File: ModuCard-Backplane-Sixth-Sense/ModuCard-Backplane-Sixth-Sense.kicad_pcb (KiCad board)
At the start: 4 copper layers, 153.9 x 128.7 mm, 138 parts, among them J1 09031967921, J16 09031967921, J17 09031967921, J18 09031967921, J19 09031967921, J2 09031967921, J20 09031967921, J21 09031967921, J6 Conn_01x02_Pin, SW1 SW_DIP_x02, SW2 SW_DIP_x02, SW3 SW_DIP_x02, SW4 SW_DIP_x02, U1 LM5007MM, U3 AMS1117, U4 FE2.1, U801 FSUSB42UMX, U802 FSUSB42UMX, X2 X322512MSB4SI

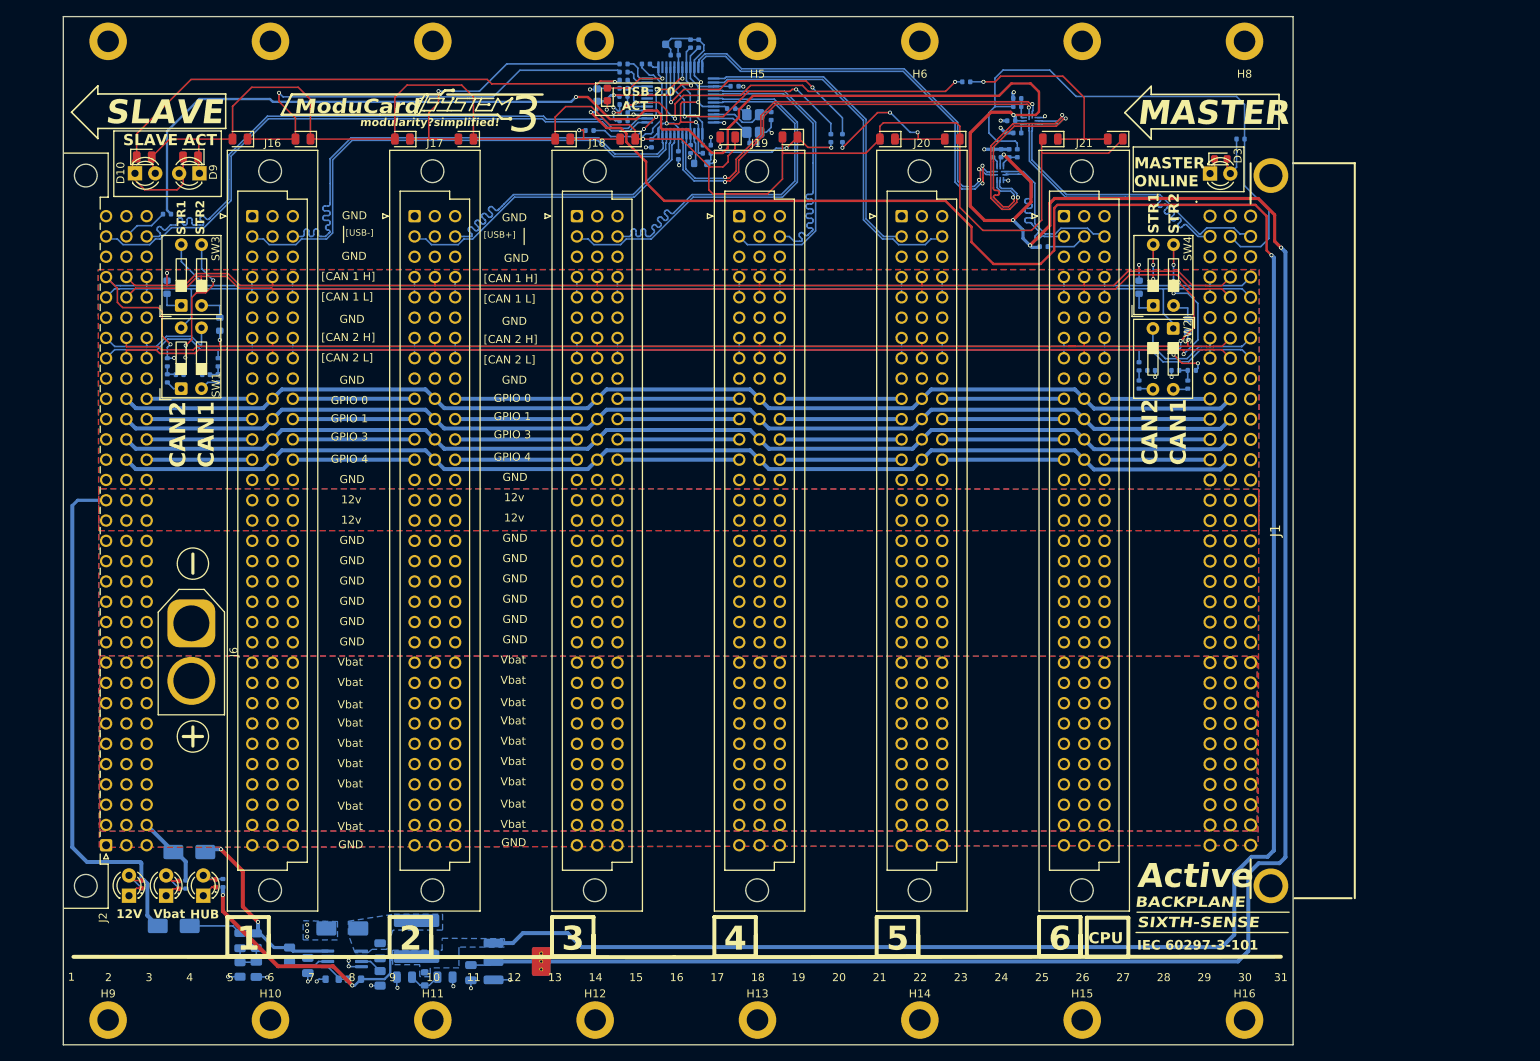
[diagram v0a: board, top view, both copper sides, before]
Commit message: fix DRC errors, change pinout
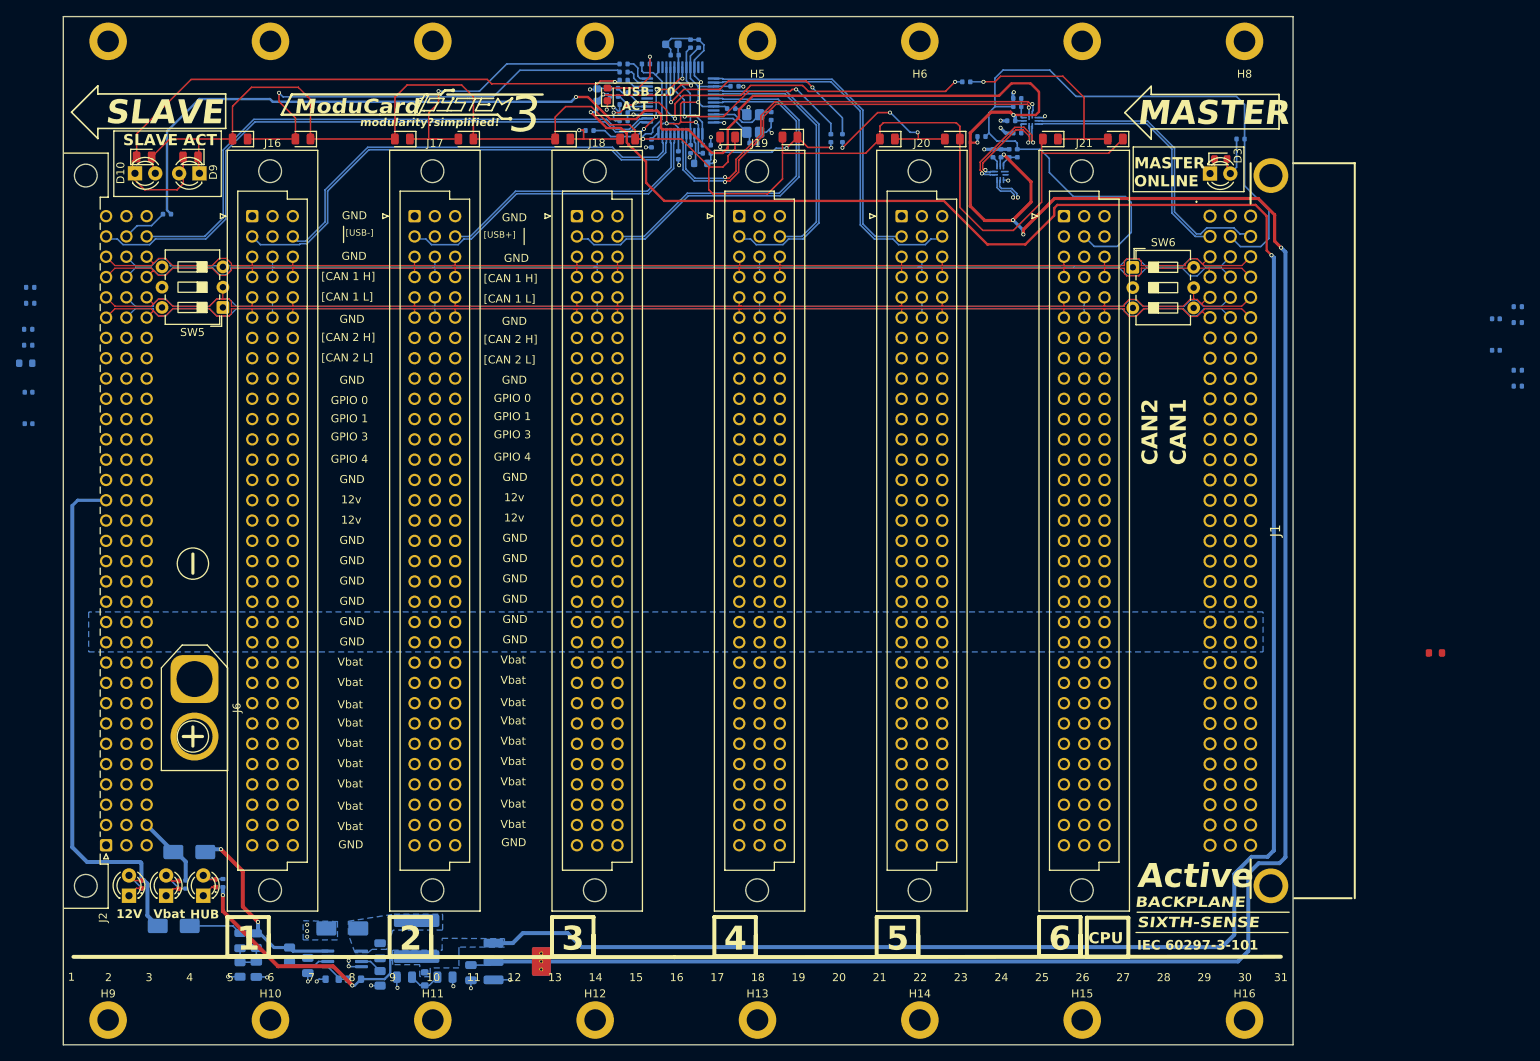
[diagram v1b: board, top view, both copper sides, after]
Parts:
- removed R21, R23: 100Ω, PCM_JLCPCB:R_0603
- removed R25: 1kΩ, PCM_JLCPCB:R_0402
- removed SW1, SW2, SW3, SW4: SW_DIP_x02, Button_Switch_THT:SW_DIP_SPSTx02_Slide_9.78x7.26mm_W7.62mm_P2.54mm
- added R2: 10kΩ, PCM_JLCPCB:R_0402, B.Cu at (204.8, 93.2)
- added R20: 10kΩ, PCM_JLCPCB:R_0402, B.Cu at (248.5, 98.8)
- added SW5: SW_DIP_x03, Button_Switch_THT:SW_DIP_SPSTx03_Slide_6.7x9.18mm_W7.62mm_P2.54mm_LowProfile, F.Cu at (153.6, 120.1)
- added SW6: SW_DIP_x03, Button_Switch_THT:SW_DIP_SPSTx03_Slide_6.7x9.18mm_W7.62mm_P2.54mm_LowProfile, F.Cu at (267.4, 115.1)
- R22: moved to F.Cu
- moved R5 169.2 mm to (315.6, 122.0), turned to 180 degrees
- moved R4 169.2 mm to (315.6, 120.0), turned to 180 degrees
- moved C21 164.9 mm to (312.9, 121.6), turned to 180 degrees
- moved R8 162.7 mm to (315.6, 128.0), turned to 180 degrees
- moved R9 162.7 mm to (315.6, 130.0), turned to 180 degrees
- moved C23 161.5 mm to (312.9, 125.5)
- moved R22 157.6 mm to (305.3, 163.4), turned to 0 degrees
- moved R7 145.6 mm to (129.4, 119.6), turned to 180 degrees
- moved R24 145.5 mm to (128.9, 127.1), turned to 180 degrees
- moved R6 145.4 mm to (129.4, 117.6), turned to 180 degrees
- moved C22 143.6 mm to (129.2, 130.8)
- moved C24 140.7 mm to (129.2, 134.7), turned to 180 degrees
- moved R10 139.2 mm to (129.2, 122.9), turned to 180 degrees
- moved R11 139.1 mm to (129.2, 124.9), turned to 180 degrees
- moved J6 6.98 mm to (150.0, 166.7)
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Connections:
- D10 pad 2: Net-(D10-A) -> /FE2.1/DRV
- D20 pad 2: Net-(D10-A) -> /FE2.1/DRV
- D21 pad 1: Net-(D10-A) -> /FE2.1/DRV
- D22 pad 2: Net-(D10-A) -> /FE2.1/DRV
- D23 pad 1: Net-(D10-A) -> /FE2.1/DRV
- D24 pad 2: Net-(D10-A) -> /FE2.1/DRV
- D25 pad 1: Net-(D10-A) -> /FE2.1/DRV
- D26 pad 2: Net-(D10-A) -> /FE2.1/DRV
- D27 pad 1: Net-(D10-A) -> /FE2.1/DRV
- D28 pad 2: Net-(D10-A) -> /FE2.1/DRV
- D29 pad 1: Net-(D10-A) -> /FE2.1/DRV
- D30 pad 2: Net-(D10-A) -> /FE2.1/DRV
- D31 pad 1: Net-(D10-A) -> /FE2.1/DRV
- D32 pad 1: Net-(D10-A) -> /FE2.1/DRV
- D33 pad 2: Net-(D10-A) -> /FE2.1/DRV
- D34 pad 2: /FE2.1/DRV -> Net-(D34-Pad2)
- D9 pad 1: Net-(D10-A) -> /FE2.1/DRV
- J1 pad A10: /Ext-conn-M/GPIOL0 -> /Ext-conn-M/GPIOL3
- J1 pad A11: /Ext-conn-M/GPIOL1 -> /Ext-conn-M/GPIOL4
- J1 pad A12: /Ext-conn-M/GPIOL2 -> /Ext-conn-M/GPIOL5
- J1 pad A13: /Ext-conn-M/GPIOL3 -> /Ext-conn-M/GPIOL6
- J1 pad A14: GND -> /Ext-conn-M/GPIOL7
- J1 pad A15: +12V -> /Ext-conn-M/GPIOL8
- J1 pad A16: +12V -> /Ext-conn-M/GPIOL9
- J1 pad A17: GND -> /Ext-conn-M/GPIOL10
- J1 pad A18: GND -> /Ext-conn-M/GPIOL11
- J1 pad A19: GND -> /Ext-conn-M/GPIOL12
- J1 pad A20: GND -> /Ext-conn-M/GPIOL13
- J1 pad A21: GND -> /Ext-conn-M/GPIOL14
- J1 pad A22: GND -> /Ext-conn-M/GPIOL15
- J1 pad A23: Vbat -> GND
- J1 pad A3: GND -> /Can Split Terminators/CAN1.+
- J1 pad A4: /Can Split Terminators/CAN1.+ -> /Can Split Terminators/CAN1.-
- J1 pad A5: /Can Split Terminators/CAN1.- -> /Can Split Terminators/CAN2.+
- J1 pad A6: GND -> /Can Split Terminators/CAN2.-
- J1 pad A7: /Can Split Terminators/CAN2.+ -> /Ext-conn-M/GPIOL0
- J1 pad A8: /Can Split Terminators/CAN2.- -> /Ext-conn-M/GPIOL1
- J1 pad A9: GND -> /Ext-conn-M/GPIOL2
- J1 pad B10: /Ext-Connector/GPIOC0 -> GND
- J1 pad B11: /Ext-Connector/GPIOC1 -> GND
- J1 pad B12: /Ext-Connector/GPIOC2 -> GND
- J1 pad B13: /Ext-Connector/GPIOC3 -> GND
- J1 pad B15: +12V -> GND
- J1 pad B16: +12V -> GND
- J1 pad B23: Vbat -> GND
- J1 pad B3: GND -> /Can Split Terminators/Strobe1.+
- J1 pad B4: /Can Split Terminators/Strobe1.+ -> /Can Split Terminators/Strobe1.-
- J1 pad B5: /Can Split Terminators/Strobe1.- -> /Ext-Connector/Strobe2.+
- J1 pad B6: GND -> /Ext-Connector/Strobe2.-
- J1 pad B7: /Can Split Terminators/Strobe2.+ -> GND
- J1 pad B8: /Can Split Terminators/Strobe2.- -> GND
- J1 pad C10: /Ext-conn-M/GPIOR0 -> /Ext-conn-M/GPIOR3
- J1 pad C11: /Ext-conn-M/GPIOR1 -> /Ext-conn-M/GPIOR4
- J1 pad C12: /Ext-conn-M/GPIOR2 -> /Ext-conn-M/GPIOR5
- J1 pad C13: /Ext-conn-M/GPIOR3 -> /Ext-conn-M/GPIOR6
- J1 pad C14: GND -> /Ext-conn-M/GPIOR7
- J1 pad C15: +12V -> /Ext-conn-M/GPIOR8
- J1 pad C16: +12V -> /Ext-conn-M/GPIOR9
- J1 pad C17: GND -> /Ext-conn-M/GPIOR10
- J1 pad C18: GND -> /Ext-conn-M/GPIOR11
- J1 pad C19: GND -> /Ext-conn-M/GPIOR12
- J1 pad C20: GND -> /Ext-conn-M/GPIOR13
- J1 pad C21: GND -> /Ext-conn-M/GPIOR14
- J1 pad C22: GND -> /Ext-conn-M/GPIOR15
- J1 pad C23: Vbat -> GND
- J1 pad C3: GND -> /Can Split Terminators/CAN1.+
- J1 pad C4: /Can Split Terminators/CAN1.+ -> /Can Split Terminators/CAN1.-
- J1 pad C5: /Can Split Terminators/CAN1.- -> /Can Split Terminators/CAN2.+
- J1 pad C6: GND -> /Can Split Terminators/CAN2.-
- J1 pad C7: /Can Split Terminators/CAN2.+ -> /Ext-conn-M/GPIOR0
- J1 pad C8: /Can Split Terminators/CAN2.- -> /Ext-conn-M/GPIOR1
- J1 pad C9: GND -> /Ext-conn-M/GPIOR2
- J16 pad a10: /Ext-Connector/GPIOR0 -> /Ext-Connector/GPIOR3
- J16 pad a11: /Ext-Connector/GPIOR1 -> /Ext-Connector/GPIOR4
- J16 pad a12: /Ext-Connector/GPIOR2 -> /Ext-Connector/GPIOR5
- J16 pad a13: /Ext-Connector/GPIOR3 -> /Ext-Connector/GPIOR6
- J16 pad a14: GND -> /Ext-Connector/GPIOR7
- J16 pad a15: +12V -> /Ext-Connector/GPIOR8
- J16 pad a16: +12V -> /Ext-Connector/GPIOR9
- J16 pad a17: GND -> /Ext-Connector/GPIOR10
- J16 pad a18: GND -> /Ext-Connector/GPIOR11
- J16 pad a19: GND -> /Ext-Connector/GPIOR12
- J16 pad a20: GND -> /Ext-Connector/GPIOR13
- J16 pad a21: GND -> /Ext-Connector/GPIOR14
- J16 pad a22: GND -> /Ext-Connector/GPIOR15
- J16 pad a23: Vbat -> GND
- J16 pad a3: GND -> /Can Split Terminators/CAN1.+
- J16 pad a4: /Can Split Terminators/CAN1.+ -> /Can Split Terminators/CAN1.-
- J16 pad a5: /Can Split Terminators/CAN1.- -> /Can Split Terminators/CAN2.+
- J16 pad a6: GND -> /Can Split Terminators/CAN2.-
- J16 pad a7: /Can Split Terminators/CAN2.+ -> /Ext-Connector/GPIOR0
- J16 pad a8: /Can Split Terminators/CAN2.- -> /Ext-Connector/GPIOR1
- J16 pad a9: GND -> /Ext-Connector/GPIOR2
- J16 pad b10: /Ext-Connector/GPIOC0 -> GND
- J16 pad b11: /Ext-Connector/GPIOC1 -> GND
- J16 pad b12: /Ext-Connector/GPIOC2 -> GND
- J16 pad b13: /Ext-Connector/GPIOC3 -> GND
- J16 pad b15: +12V -> GND
- J16 pad b16: +12V -> GND
- J16 pad b23: Vbat -> GND
- J16 pad b3: GND -> /Can Split Terminators/Strobe1.+
- J16 pad b4: /Can Split Terminators/Strobe1.+ -> /Can Split Terminators/Strobe1.-
- J16 pad b5: /Can Split Terminators/Strobe1.- -> /Ext-Connector/Strobe2.+
- J16 pad b6: GND -> /Ext-Connector/Strobe2.-
- J16 pad b7: /Can Split Terminators/Strobe2.+ -> GND
- J16 pad b8: /Can Split Terminators/Strobe2.- -> GND
- J16 pad c10: /Port1/GPIOR0 -> /Port1/GPIOR3
- J16 pad c11: /Port1/GPIOR1 -> /Port1/GPIOR4
- J16 pad c12: /Port1/GPIOR2 -> /Port1/GPIOR5
- J16 pad c13: /Port1/GPIOR3 -> /Port1/GPIOR6
- J16 pad c14: GND -> /Port1/GPIOR7
- J16 pad c15: +12V -> /Port1/GPIOR8
- J16 pad c16: +12V -> /Port1/GPIOR9
- J16 pad c17: GND -> /Port1/GPIOR10
- J16 pad c18: GND -> /Port1/GPIOR11
- J16 pad c19: GND -> /Port1/GPIOR12
- J16 pad c20: GND -> /Port1/GPIOR13
- J16 pad c21: GND -> /Port1/GPIOR14
- J16 pad c22: GND -> /Port1/GPIOR15
- J16 pad c23: Vbat -> GND
- J16 pad c3: GND -> /Can Split Terminators/CAN1.+
- J16 pad c4: /Can Split Terminators/CAN1.+ -> /Can Split Terminators/CAN1.-
- J16 pad c5: /Can Split Terminators/CAN1.- -> /Can Split Terminators/CAN2.+
- J16 pad c6: GND -> /Can Split Terminators/CAN2.-
- J16 pad c7: /Can Split Terminators/CAN2.+ -> /Port1/GPIOR0
- J16 pad c8: /Can Split Terminators/CAN2.- -> /Port1/GPIOR1
- J16 pad c9: GND -> /Port1/GPIOR2
- J17 pad a10: /Port1/GPIOR0 -> /Port1/GPIOR3
- J17 pad a11: /Port1/GPIOR1 -> /Port1/GPIOR4
- J17 pad a12: /Port1/GPIOR2 -> /Port1/GPIOR5
- J17 pad a13: /Port1/GPIOR3 -> /Port1/GPIOR6
- J17 pad a14: GND -> /Port1/GPIOR7
- J17 pad a15: +12V -> /Port1/GPIOR8
- J17 pad a16: +12V -> /Port1/GPIOR9
- J17 pad a17: GND -> /Port1/GPIOR10
- J17 pad a18: GND -> /Port1/GPIOR11
- J17 pad a19: GND -> /Port1/GPIOR12
- J17 pad a20: GND -> /Port1/GPIOR13
- J17 pad a21: GND -> /Port1/GPIOR14
- J17 pad a22: GND -> /Port1/GPIOR15
- J17 pad a23: Vbat -> GND
- J17 pad a3: GND -> /Can Split Terminators/CAN1.+
- J17 pad a4: /Can Split Terminators/CAN1.+ -> /Can Split Terminators/CAN1.-
- J17 pad a5: /Can Split Terminators/CAN1.- -> /Can Split Terminators/CAN2.+
- J17 pad a6: GND -> /Can Split Terminators/CAN2.-
- J17 pad a7: /Can Split Terminators/CAN2.+ -> /Port1/GPIOR0
- J17 pad a8: /Can Split Terminators/CAN2.- -> /Port1/GPIOR1
- J17 pad a9: GND -> /Port1/GPIOR2
- J17 pad b10: /Ext-Connector/GPIOC0 -> GND
- J17 pad b11: /Ext-Connector/GPIOC1 -> GND
- J17 pad b12: /Ext-Connector/GPIOC2 -> GND
- J17 pad b13: /Ext-Connector/GPIOC3 -> GND
- J17 pad b15: +12V -> GND
- J17 pad b16: +12V -> GND
- J17 pad b23: Vbat -> GND
- J17 pad b3: GND -> /Can Split Terminators/Strobe1.+
- J17 pad b4: /Can Split Terminators/Strobe1.+ -> /Can Split Terminators/Strobe1.-
- J17 pad b5: /Can Split Terminators/Strobe1.- -> /Ext-Connector/Strobe2.+
- J17 pad b6: GND -> /Ext-Connector/Strobe2.-
- J17 pad b7: /Can Split Terminators/Strobe2.+ -> GND
- J17 pad b8: /Can Split Terminators/Strobe2.- -> GND
- J17 pad c10: /Port2/GPIOR0 -> /Port2/GPIOR3
- J17 pad c11: /Port2/GPIOR1 -> /Port2/GPIOR4
- J17 pad c12: /Port2/GPIOR2 -> /Port2/GPIOR5
- J17 pad c13: /Port2/GPIOR3 -> /Port2/GPIOR6
- J17 pad c14: GND -> /Port2/GPIOR7
- J17 pad c15: +12V -> /Port2/GPIOR8
- J17 pad c16: +12V -> /Port2/GPIOR9
- J17 pad c17: GND -> /Port2/GPIOR10
- J17 pad c18: GND -> /Port2/GPIOR11
- J17 pad c19: GND -> /Port2/GPIOR12
- J17 pad c20: GND -> /Port2/GPIOR13
- J17 pad c21: GND -> /Port2/GPIOR14
- J17 pad c22: GND -> /Port2/GPIOR15
- J17 pad c23: Vbat -> GND
- J17 pad c3: GND -> /Can Split Terminators/CAN1.+
- J17 pad c4: /Can Split Terminators/CAN1.+ -> /Can Split Terminators/CAN1.-
- J17 pad c5: /Can Split Terminators/CAN1.- -> /Can Split Terminators/CAN2.+
- J17 pad c6: GND -> /Can Split Terminators/CAN2.-
- J17 pad c7: /Can Split Terminators/CAN2.+ -> /Port2/GPIOR0
- J17 pad c8: /Can Split Terminators/CAN2.- -> /Port2/GPIOR1
- J17 pad c9: GND -> /Port2/GPIOR2
- J18 pad a10: /Port2/GPIOR0 -> /Port2/GPIOR3
- J18 pad a11: /Port2/GPIOR1 -> /Port2/GPIOR4
- J18 pad a12: /Port2/GPIOR2 -> /Port2/GPIOR5
- J18 pad a13: /Port2/GPIOR3 -> /Port2/GPIOR6
- J18 pad a14: GND -> /Port2/GPIOR7
- J18 pad a15: +12V -> /Port2/GPIOR8
- J18 pad a16: +12V -> /Port2/GPIOR9
- J18 pad a17: GND -> /Port2/GPIOR10
- J18 pad a18: GND -> /Port2/GPIOR11
- J18 pad a19: GND -> /Port2/GPIOR12
- J18 pad a20: GND -> /Port2/GPIOR13
- J18 pad a21: GND -> /Port2/GPIOR14
- J18 pad a22: GND -> /Port2/GPIOR15
- J18 pad a23: Vbat -> GND
- J18 pad a3: GND -> /Can Split Terminators/CAN1.+
- J18 pad a4: /Can Split Terminators/CAN1.+ -> /Can Split Terminators/CAN1.-
- J18 pad a5: /Can Split Terminators/CAN1.- -> /Can Split Terminators/CAN2.+
- J18 pad a6: GND -> /Can Split Terminators/CAN2.-
- J18 pad a7: /Can Split Terminators/CAN2.+ -> /Port2/GPIOR0
- J18 pad a8: /Can Split Terminators/CAN2.- -> /Port2/GPIOR1
- J18 pad a9: GND -> /Port2/GPIOR2
- J18 pad b10: /Ext-Connector/GPIOC0 -> GND
- J18 pad b11: /Ext-Connector/GPIOC1 -> GND
- J18 pad b12: /Ext-Connector/GPIOC2 -> GND
- J18 pad b13: /Ext-Connector/GPIOC3 -> GND
- J18 pad b15: +12V -> GND
- J18 pad b16: +12V -> GND
- J18 pad b23: Vbat -> GND
- J18 pad b3: GND -> /Can Split Terminators/Strobe1.+
- J18 pad b4: /Can Split Terminators/Strobe1.+ -> /Can Split Terminators/Strobe1.-
- J18 pad b5: /Can Split Terminators/Strobe1.- -> /Ext-Connector/Strobe2.+
- J18 pad b6: GND -> /Ext-Connector/Strobe2.-
- J18 pad b7: /Can Split Terminators/Strobe2.+ -> GND
- J18 pad b8: /Can Split Terminators/Strobe2.- -> GND
- J18 pad c10: /Port3/GPIOR0 -> /Port3/GPIOR3
- J18 pad c11: /Port3/GPIOR1 -> /Port3/GPIOR4
- J18 pad c12: /Port3/GPIOR2 -> /Port3/GPIOR5
- J18 pad c13: /Port3/GPIOR3 -> /Port3/GPIOR6
- J18 pad c14: GND -> /Port3/GPIOR7
- J18 pad c15: +12V -> /Port3/GPIOR8
- J18 pad c16: +12V -> /Port3/GPIOR9
- J18 pad c17: GND -> /Port3/GPIOR10
- J18 pad c18: GND -> /Port3/GPIOR11
- J18 pad c19: GND -> /Port3/GPIOR12
- J18 pad c20: GND -> /Port3/GPIOR13
- J18 pad c21: GND -> /Port3/GPIOR14
- J18 pad c22: GND -> /Port3/GPIOR15
- J18 pad c23: Vbat -> GND
- J18 pad c3: GND -> /Can Split Terminators/CAN1.+
- J18 pad c4: /Can Split Terminators/CAN1.+ -> /Can Split Terminators/CAN1.-
- J18 pad c5: /Can Split Terminators/CAN1.- -> /Can Split Terminators/CAN2.+
- J18 pad c6: GND -> /Can Split Terminators/CAN2.-
- J18 pad c7: /Can Split Terminators/CAN2.+ -> /Port3/GPIOR0
- J18 pad c8: /Can Split Terminators/CAN2.- -> /Port3/GPIOR1
- J18 pad c9: GND -> /Port3/GPIOR2
- J19 pad a10: /Port3/GPIOR0 -> /Port3/GPIOR3
- J19 pad a11: /Port3/GPIOR1 -> /Port3/GPIOR4
- J19 pad a12: /Port3/GPIOR2 -> /Port3/GPIOR5
- J19 pad a13: /Port3/GPIOR3 -> /Port3/GPIOR6
- J19 pad a14: GND -> /Port3/GPIOR7
- J19 pad a15: +12V -> /Port3/GPIOR8
- J19 pad a16: +12V -> /Port3/GPIOR9
- J19 pad a17: GND -> /Port3/GPIOR10
- J19 pad a18: GND -> /Port3/GPIOR11
- J19 pad a19: GND -> /Port3/GPIOR12
- J19 pad a20: GND -> /Port3/GPIOR13
- J19 pad a21: GND -> /Port3/GPIOR14
- J19 pad a22: GND -> /Port3/GPIOR15
- J19 pad a23: Vbat -> GND
- J19 pad a3: GND -> /Can Split Terminators/CAN1.+
- J19 pad a4: /Can Split Terminators/CAN1.+ -> /Can Split Terminators/CAN1.-
- J19 pad a5: /Can Split Terminators/CAN1.- -> /Can Split Terminators/CAN2.+
- J19 pad a6: GND -> /Can Split Terminators/CAN2.-
- J19 pad a7: /Can Split Terminators/CAN2.+ -> /Port3/GPIOR0
- J19 pad a8: /Can Split Terminators/CAN2.- -> /Port3/GPIOR1
- J19 pad a9: GND -> /Port3/GPIOR2
- J19 pad b10: /Ext-Connector/GPIOC0 -> GND
- J19 pad b11: /Ext-Connector/GPIOC1 -> GND
- J19 pad b12: /Ext-Connector/GPIOC2 -> GND
- J19 pad b13: /Ext-Connector/GPIOC3 -> GND
- J19 pad b15: +12V -> GND
- J19 pad b16: +12V -> GND
- J19 pad b23: Vbat -> GND
- J19 pad b3: GND -> /Can Split Terminators/Strobe1.+
- J19 pad b4: /Can Split Terminators/Strobe1.+ -> /Can Split Terminators/Strobe1.-
- J19 pad b5: /Can Split Terminators/Strobe1.- -> /Ext-Connector/Strobe2.+
- J19 pad b6: GND -> /Ext-Connector/Strobe2.-
- J19 pad b7: /Can Split Terminators/Strobe2.+ -> GND
- J19 pad b8: /Can Split Terminators/Strobe2.- -> GND
- J19 pad c10: /Port4/GPIOR0 -> /Port4/GPIOR3
- J19 pad c11: /Port4/GPIOR1 -> /Port4/GPIOR4
- J19 pad c12: /Port4/GPIOR2 -> /Port4/GPIOR5
- J19 pad c13: /Port4/GPIOR3 -> /Port4/GPIOR6
- J19 pad c14: GND -> /Port4/GPIOR7
- J19 pad c15: +12V -> /Port4/GPIOR8
- J19 pad c16: +12V -> /Port4/GPIOR9
- J19 pad c17: GND -> /Port4/GPIOR10
- J19 pad c18: GND -> /Port4/GPIOR11
- J19 pad c19: GND -> /Port4/GPIOR12
- J19 pad c20: GND -> /Port4/GPIOR13
- J19 pad c21: GND -> /Port4/GPIOR14
- J19 pad c22: GND -> /Port4/GPIOR15
- J19 pad c23: Vbat -> GND
- J19 pad c3: GND -> /Can Split Terminators/CAN1.+
- J19 pad c4: /Can Split Terminators/CAN1.+ -> /Can Split Terminators/CAN1.-
- J19 pad c5: /Can Split Terminators/CAN1.- -> /Can Split Terminators/CAN2.+
- J19 pad c6: GND -> /Can Split Terminators/CAN2.-
- J19 pad c7: /Can Split Terminators/CAN2.+ -> /Port4/GPIOR0
- J19 pad c8: /Can Split Terminators/CAN2.- -> /Port4/GPIOR1
- J19 pad c9: GND -> /Port4/GPIOR2
- J2 pad a10: Vbat -> GND
- J2 pad a11: GND -> /Ext-Connector/GPIOL15
- J2 pad a12: GND -> /Ext-Connector/GPIOL14
- J2 pad a13: GND -> /Ext-Connector/GPIOL13
- J2 pad a14: GND -> /Ext-Connector/GPIOL12
- J2 pad a15: GND -> /Ext-Connector/GPIOL11
- J2 pad a16: GND -> /Ext-Connector/GPIOL10
- J2 pad a17: +12V -> /Ext-Connector/GPIOL9
- J2 pad a18: +12V -> /Ext-Connector/GPIOL8
- J2 pad a19: GND -> /Ext-Connector/GPIOL7
- J2 pad a20: /Ext-Connector/GPIOL3 -> /Ext-Connector/GPIOL6
- J2 pad a21: /Ext-Connector/GPIOL2 -> /Ext-Connector/GPIOL5
- J2 pad a22: /Ext-Connector/GPIOL1 -> /Ext-Connector/GPIOL4
- J2 pad a23: /Ext-Connector/GPIOL0 -> /Ext-Connector/GPIOL3
- J2 pad a24: GND -> /Ext-Connector/GPIOL2
- J2 pad a25: /Can Split Terminators/CAN2.- -> /Ext-Connector/GPIOL1
- J2 pad a26: /Can Split Terminators/CAN2.+ -> /Ext-Connector/GPIOL0
- J2 pad a27: GND -> /Can Split Terminators/CAN2.-
- J2 pad a28: /Can Split Terminators/CAN1.- -> /Can Split Terminators/CAN2.+
- J2 pad a29: /Can Split Terminators/CAN1.+ -> /Can Split Terminators/CAN1.-
- J2 pad a30: GND -> /Can Split Terminators/CAN1.+
- J2 pad b10: Vbat -> GND
- J2 pad b17: +12V -> GND
- J2 pad b18: +12V -> GND
- J2 pad b20: /Ext-Connector/GPIOC3 -> GND
- J2 pad b21: /Ext-Connector/GPIOC2 -> GND
- J2 pad b22: /Ext-Connector/GPIOC1 -> GND
- J2 pad b23: /Ext-Connector/GPIOC0 -> GND
- J2 pad b25: /Can Split Terminators/Strobe2.- -> GND
- J2 pad b26: /Can Split Terminators/Strobe2.+ -> GND
- J2 pad b27: GND -> /Ext-Connector/Strobe2.-
- J2 pad b28: /Can Split Terminators/Strobe1.- -> /Ext-Connector/Strobe2.+
- J2 pad b29: /Can Split Terminators/Strobe1.+ -> /Can Split Terminators/Strobe1.-
- J2 pad b30: GND -> /Can Split Terminators/Strobe1.+
- J2 pad c10: Vbat -> GND
- J2 pad c11: GND -> /Ext-Connector/GPIOR15
- J2 pad c12: GND -> /Ext-Connector/GPIOR14
- J2 pad c13: GND -> /Ext-Connector/GPIOR13
- J2 pad c14: GND -> /Ext-Connector/GPIOR12
- J2 pad c15: GND -> /Ext-Connector/GPIOR11
- J2 pad c16: GND -> /Ext-Connector/GPIOR10
- J2 pad c17: +12V -> /Ext-Connector/GPIOR9
- J2 pad c18: +12V -> /Ext-Connector/GPIOR8
- J2 pad c19: GND -> /Ext-Connector/GPIOR7
- J2 pad c20: /Ext-Connector/GPIOR3 -> /Ext-Connector/GPIOR6
- J2 pad c21: /Ext-Connector/GPIOR2 -> /Ext-Connector/GPIOR5
- J2 pad c22: /Ext-Connector/GPIOR1 -> /Ext-Connector/GPIOR4
- J2 pad c23: /Ext-Connector/GPIOR0 -> /Ext-Connector/GPIOR3
- J2 pad c24: GND -> /Ext-Connector/GPIOR2
- J2 pad c25: /Can Split Terminators/CAN2.- -> /Ext-Connector/GPIOR1
- J2 pad c26: /Can Split Terminators/CAN2.+ -> /Ext-Connector/GPIOR0
- J2 pad c27: GND -> /Can Split Terminators/CAN2.-
- J2 pad c28: /Can Split Terminators/CAN1.- -> /Can Split Terminators/CAN2.+
- J2 pad c29: /Can Split Terminators/CAN1.+ -> /Can Split Terminators/CAN1.-
- J2 pad c30: GND -> /Can Split Terminators/CAN1.+
- J20 pad a10: /Port4/GPIOR0 -> /Port4/GPIOR3
- J20 pad a11: /Port4/GPIOR1 -> /Port4/GPIOR4
- J20 pad a12: /Port4/GPIOR2 -> /Port4/GPIOR5
- J20 pad a13: /Port4/GPIOR3 -> /Port4/GPIOR6
- J20 pad a14: GND -> /Port4/GPIOR7
- J20 pad a15: +12V -> /Port4/GPIOR8
- J20 pad a16: +12V -> /Port4/GPIOR9
- J20 pad a17: GND -> /Port4/GPIOR10
- J20 pad a18: GND -> /Port4/GPIOR11
- J20 pad a19: GND -> /Port4/GPIOR12
- J20 pad a20: GND -> /Port4/GPIOR13
- J20 pad a21: GND -> /Port4/GPIOR14
- J20 pad a22: GND -> /Port4/GPIOR15
- J20 pad a23: Vbat -> GND
- J20 pad a3: GND -> /Can Split Terminators/CAN1.+
- J20 pad a4: /Can Split Terminators/CAN1.+ -> /Can Split Terminators/CAN1.-
- J20 pad a5: /Can Split Terminators/CAN1.- -> /Can Split Terminators/CAN2.+
- J20 pad a6: GND -> /Can Split Terminators/CAN2.-
- J20 pad a7: /Can Split Terminators/CAN2.+ -> /Port4/GPIOR0
- J20 pad a8: /Can Split Terminators/CAN2.- -> /Port4/GPIOR1
- J20 pad a9: GND -> /Port4/GPIOR2
- J20 pad b10: /Ext-Connector/GPIOC0 -> GND
- J20 pad b11: /Ext-Connector/GPIOC1 -> GND
- J20 pad b12: /Ext-Connector/GPIOC2 -> GND
- J20 pad b13: /Ext-Connector/GPIOC3 -> GND
- J20 pad b15: +12V -> GND
- J20 pad b16: +12V -> GND
- J20 pad b23: Vbat -> GND
- J20 pad b3: GND -> /Can Split Terminators/Strobe1.+
- J20 pad b4: /Can Split Terminators/Strobe1.+ -> /Can Split Terminators/Strobe1.-
- J20 pad b5: /Can Split Terminators/Strobe1.- -> /Ext-Connector/Strobe2.+
- J20 pad b6: GND -> /Ext-Connector/Strobe2.-
- J20 pad b7: /Can Split Terminators/Strobe2.+ -> GND
- J20 pad b8: /Can Split Terminators/Strobe2.- -> GND
- J20 pad c10: /Port5/GPIOR0 -> /Port5/GPIOR3
- J20 pad c11: /Port5/GPIOR1 -> /Port5/GPIOR4
- J20 pad c12: /Port5/GPIOR2 -> /Port5/GPIOR5
- J20 pad c13: /Port5/GPIOR3 -> /Port5/GPIOR6
- J20 pad c14: GND -> /Port5/GPIOR7
- J20 pad c15: +12V -> /Port5/GPIOR8
- J20 pad c16: +12V -> /Port5/GPIOR9
- J20 pad c17: GND -> /Port5/GPIOR10
- J20 pad c18: GND -> /Port5/GPIOR11
- J20 pad c19: GND -> /Port5/GPIOR12
- J20 pad c20: GND -> /Port5/GPIOR13
- J20 pad c21: GND -> /Port5/GPIOR14
- J20 pad c22: GND -> /Port5/GPIOR15
- J20 pad c23: Vbat -> GND
- J20 pad c3: GND -> /Can Split Terminators/CAN1.+
- J20 pad c4: /Can Split Terminators/CAN1.+ -> /Can Split Terminators/CAN1.-
- J20 pad c5: /Can Split Terminators/CAN1.- -> /Can Split Terminators/CAN2.+
- J20 pad c6: GND -> /Can Split Terminators/CAN2.-
- J20 pad c7: /Can Split Terminators/CAN2.+ -> /Port5/GPIOR0
- J20 pad c8: /Can Split Terminators/CAN2.- -> /Port5/GPIOR1
- J20 pad c9: GND -> /Port5/GPIOR2
- J21 pad a10: /Port5/GPIOR0 -> /Port5/GPIOR3
- J21 pad a11: /Port5/GPIOR1 -> /Port5/GPIOR4
- J21 pad a12: /Port5/GPIOR2 -> /Port5/GPIOR5
- J21 pad a13: /Port5/GPIOR3 -> /Port5/GPIOR6
- J21 pad a14: GND -> /Port5/GPIOR7
- J21 pad a15: +12V -> /Port5/GPIOR8
- J21 pad a16: +12V -> /Port5/GPIOR9
- J21 pad a17: GND -> /Port5/GPIOR10
- J21 pad a18: GND -> /Port5/GPIOR11
- J21 pad a19: GND -> /Port5/GPIOR12
- J21 pad a20: GND -> /Port5/GPIOR13
- J21 pad a21: GND -> /Port5/GPIOR14
- J21 pad a22: GND -> /Port5/GPIOR15
- J21 pad a23: Vbat -> GND
- J21 pad a3: GND -> /Can Split Terminators/CAN1.+
- J21 pad a4: /Can Split Terminators/CAN1.+ -> /Can Split Terminators/CAN1.-
- J21 pad a5: /Can Split Terminators/CAN1.- -> /Can Split Terminators/CAN2.+
- J21 pad a6: GND -> /Can Split Terminators/CAN2.-
- J21 pad a7: /Can Split Terminators/CAN2.+ -> /Port5/GPIOR0
- J21 pad a8: /Can Split Terminators/CAN2.- -> /Port5/GPIOR1
- J21 pad a9: GND -> /Port5/GPIOR2
- J21 pad b10: /Ext-Connector/GPIOC0 -> GND
- J21 pad b11: /Ext-Connector/GPIOC1 -> GND
- J21 pad b12: /Ext-Connector/GPIOC2 -> GND
- J21 pad b13: /Ext-Connector/GPIOC3 -> GND
- J21 pad b15: +12V -> GND
- J21 pad b16: +12V -> GND
- J21 pad b2: /Port6/Index -> /Ext-conn-M/Index
- J21 pad b23: Vbat -> GND
- J21 pad b3: GND -> /Can Split Terminators/Strobe1.+
- J21 pad b4: /Can Split Terminators/Strobe1.+ -> /Can Split Terminators/Strobe1.-
- J21 pad b5: /Can Split Terminators/Strobe1.- -> /Ext-Connector/Strobe2.+
- J21 pad b6: GND -> /Ext-Connector/Strobe2.-
- J21 pad b7: /Can Split Terminators/Strobe2.+ -> GND
- J21 pad b8: /Can Split Terminators/Strobe2.- -> GND
- J21 pad c10: /Ext-conn-M/GPIOR0 -> /Ext-conn-M/GPIOL3
- J21 pad c11: /Ext-conn-M/GPIOR1 -> /Ext-conn-M/GPIOL4
- J21 pad c12: /Ext-conn-M/GPIOR2 -> /Ext-conn-M/GPIOL5
- J21 pad c13: /Ext-conn-M/GPIOR3 -> /Ext-conn-M/GPIOL6
- J21 pad c14: GND -> /Ext-conn-M/GPIOL7
- J21 pad c15: +12V -> /Ext-conn-M/GPIOL8
- J21 pad c16: +12V -> /Ext-conn-M/GPIOL9
- J21 pad c17: GND -> /Ext-conn-M/GPIOL10
- J21 pad c18: GND -> /Ext-conn-M/GPIOL11
- J21 pad c19: GND -> /Ext-conn-M/GPIOL12
- J21 pad c20: GND -> /Ext-conn-M/GPIOL13
- J21 pad c21: GND -> /Ext-conn-M/GPIOL14
- J21 pad c22: GND -> /Ext-conn-M/GPIOL15
- J21 pad c23: Vbat -> GND
- J21 pad c3: GND -> /Can Split Terminators/CAN1.+
- J21 pad c4: /Can Split Terminators/CAN1.+ -> /Can Split Terminators/CAN1.-
- J21 pad c5: /Can Split Terminators/CAN1.- -> /Can Split Terminators/CAN2.+
- J21 pad c6: GND -> /Can Split Terminators/CAN2.-
- J21 pad c7: /Can Split Terminators/CAN2.+ -> /Ext-conn-M/GPIOL0
- J21 pad c8: /Can Split Terminators/CAN2.- -> /Ext-conn-M/GPIOL1
- J21 pad c9: GND -> /Ext-conn-M/GPIOL2
- R22 pad 2: /Can Split Terminators/Strobe2.+ -> /Can Split Terminators/Strobe1.-
- R24 pad 2: /Can Split Terminators/Strobe2.+ -> /Can Split Terminators/Strobe1.-
- R26 pad 2: +3V3 -> GND
- R38 pad 1: Net-(D10-A) -> /FE2.1/DRV
- R38 pad 2: /FE2.1/DRV -> Net-(D34-Pad2)
- U4 pad 21: /FE2.1/VD_DLL -> /FE2.1/VD18
- U801 pad 4: /USB_MUX/USB1.D- -> /Ext-conn-M/USB.D-
- U801 pad 5: /USB_MUX/USB1.D+ -> /Ext-conn-M/USB.D+
- U801 pad 6: /Ext-conn-M/USB.D- -> /USB_MUX/USB2.D-
- U801 pad 7: /Ext-conn-M/USB.D+ -> /USB_MUX/USB2.D+
- U802 pad 4: /USB_MUX/USB1.D- -> /FE2.1/USB4.D-
- U802 pad 5: /USB_MUX/USB1.D+ -> /FE2.1/USB4.D+
- U802 pad 6: /FE2.1/USB4.D- -> /USB_MUX/USB2.D-
- U802 pad 7: /FE2.1/USB4.D+ -> /USB_MUX/USB2.D+
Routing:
- net Net-(D10-A): track 212.7 -> 0.00 mm, vias 1 -> 0
- net /FE2.1/DRV: track 10.9 -> 213.3 mm
- net /Can Split Terminators/Strobe2.-: track 182.0 -> 0.00 mm, vias 7 -> 0
- net /Can Split Terminators/Strobe2.+: track 151.0 -> 0.00 mm, vias 2 -> 0
- net /Ext-Connector/Strobe2.+: track 0.00 -> 149.6 mm
- net /Ext-Connector/Strobe2.-: track 0.00 -> 149.5 mm
- net /Ext-Connector/GPIOC1: track 145.0 -> 0.00 mm
- net /Ext-Connector/GPIOC0: track 145.0 -> 0.00 mm
- net /Ext-Connector/GPIOC2: track 145.0 -> 0.00 mm
- net /Ext-Connector/GPIOC3: track 145.0 -> 0.00 mm
- net /FE2.1/USB4.D+: track 52.0 -> 4.13 mm, vias 2 -> 1
- net /FE2.1/USB4.D-: track 52.0 -> 4.16 mm, vias 2 -> 1
- net /Ext-conn-M/Index: track 71.6 -> 101.1 mm
- net /USB_MUX/USB1.D-: track 29.5 -> 0.00 mm, vias 2 -> 0
- net /USB_MUX/USB1.D+: track 29.4 -> 0.00 mm, vias 2 -> 0
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- removed copper zone on F.Cu, net +12V
- removed copper zone on In1.Cu, net +12V
- removed copper zone on In2.Cu, net +12V
- removed copper zone on F.Cu, net GND
- removed copper zone on B.Cu, net Vbat
- removed copper zone on F.Cu, net Vbat
- removed copper zone on In1.Cu, net Vbat
- removed copper zone on In2.Cu, net Vbat
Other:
- board text removed: "STR1"
- board text removed: "STR2"
